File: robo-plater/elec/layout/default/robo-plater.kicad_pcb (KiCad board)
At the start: 2 copper layers, 170 parts, among them J1 ?, U1 ?, U10 ?, U11 ?, U12 ?, U13 ?, U14 ?, U15 ?, U16 ?, U17 ?, U18 ?, U19 ?, U2 ?, U20 ?, U21 ?, U22 ?, U23 ?, U24 ?, U25 ?, U26 ?, U27 ?, U28 ?, U29 ?, U3 ?, U30 ?, U31 ?, U32 ?, U33 ?, U34 ?, U35 ?, U36 ?, U37 0.6A, 42V, 1.1MHz Buck Regula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, U4 ?, U5 ?, U6 ?, U7 ?, U8 ?, U9 ?

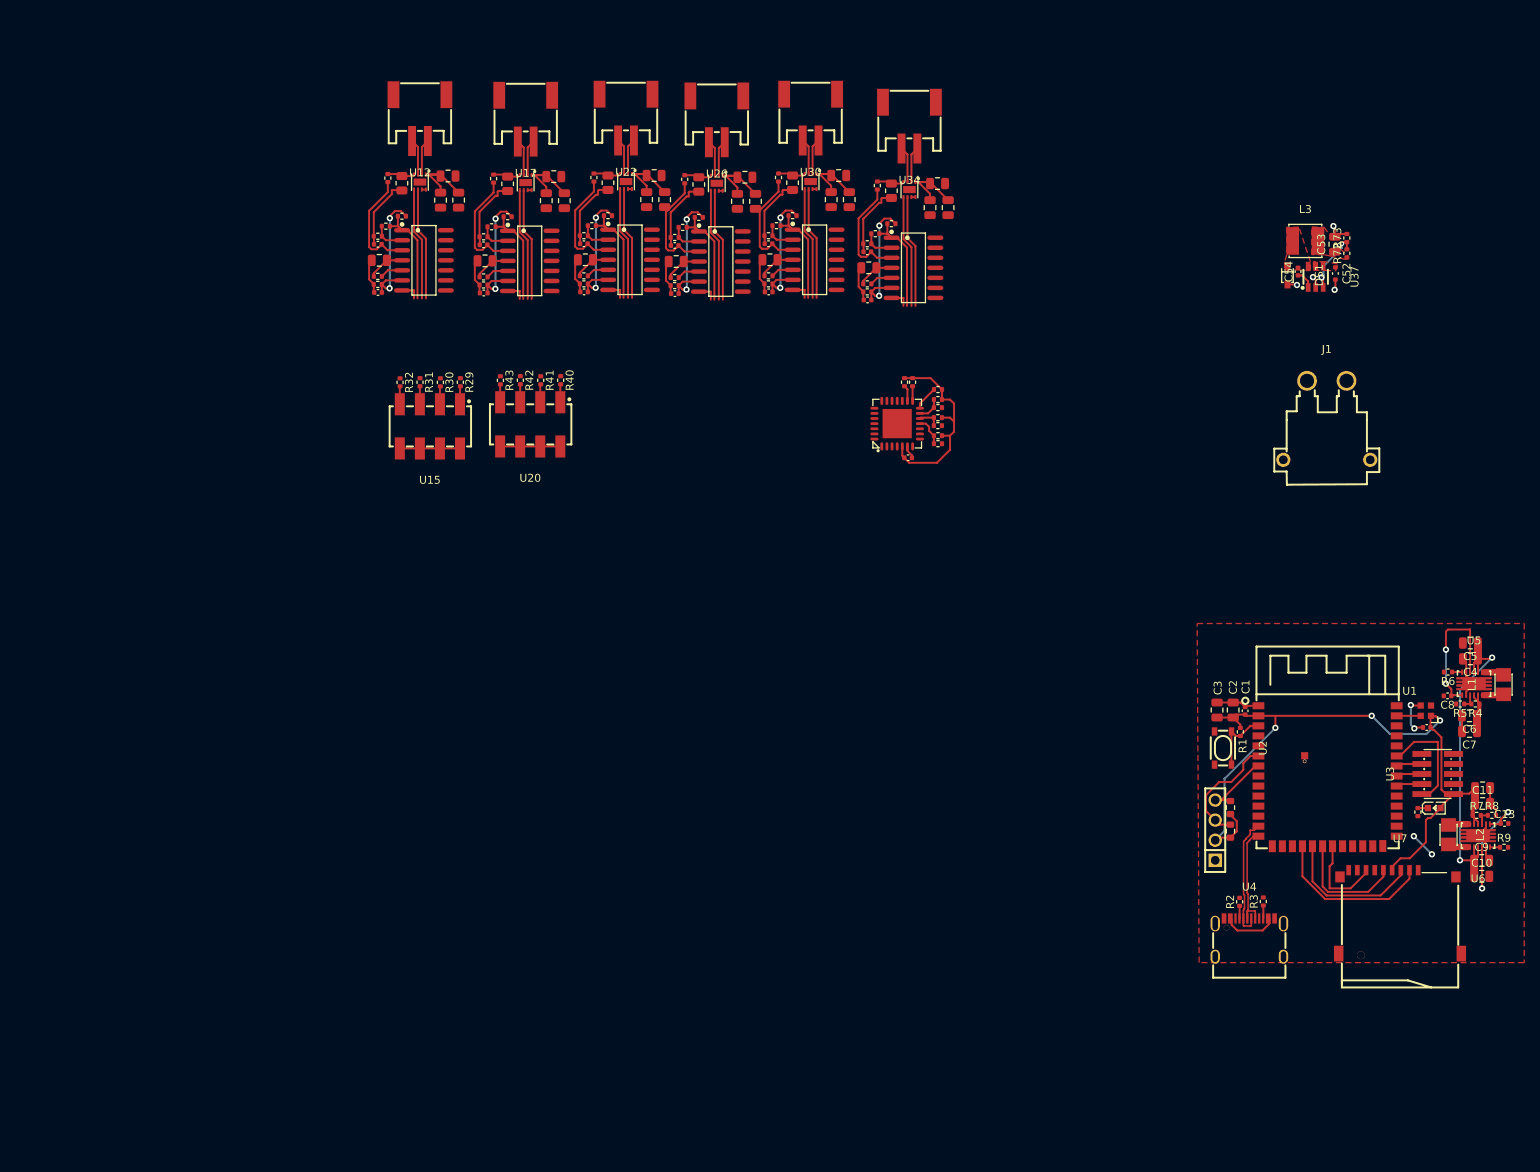
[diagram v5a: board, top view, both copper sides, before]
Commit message: Reorganise into channels
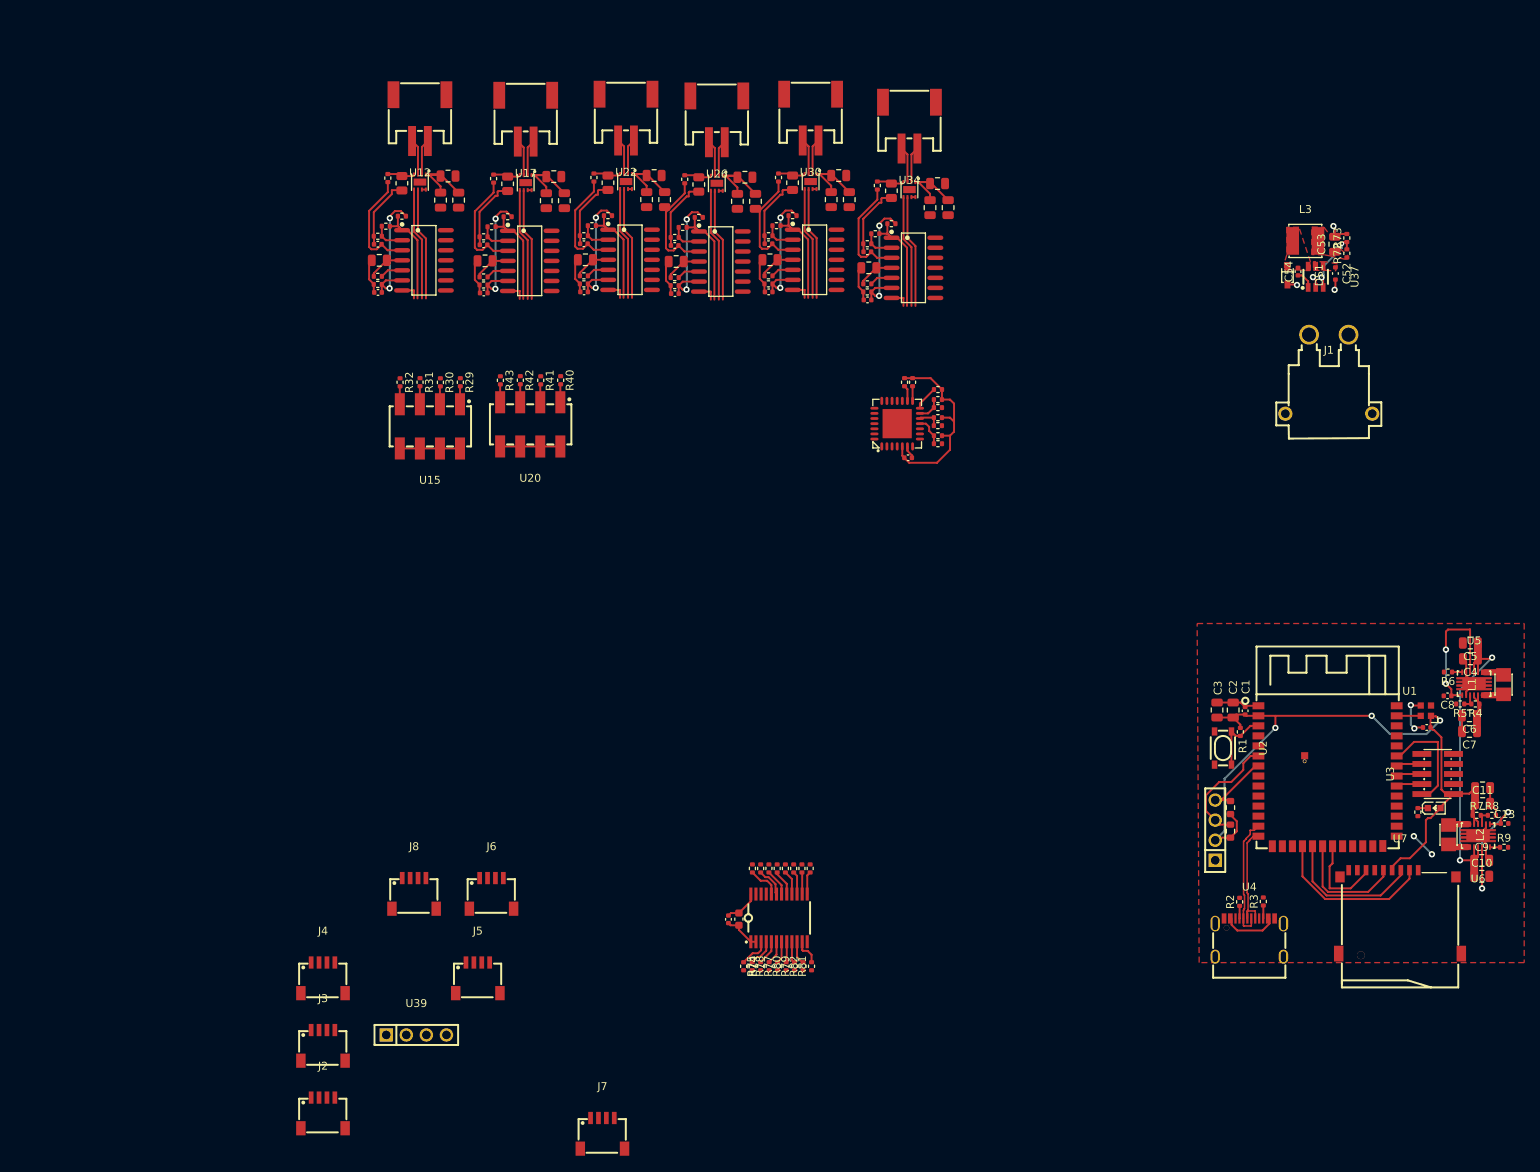
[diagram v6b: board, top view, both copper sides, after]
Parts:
- added C55: 16V 100nF X7R ±10% 0402 Multilayer Ceramic Capacitors MLCC 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, lib:C0402, F.Cu at (119.6, 149.3)
- added C56: 16V 2.2uF X5R ±10% 0603 Multilayer Ceramic Capacitors MLCC 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, lib:C0603, F.Cu at (120.9, 149.3)
- added J2: ?, lib:CONN-SMD_4P-P1.00_SM04B-SRSS-TB-LF-SN, F.Cu at (68.3, 173.8)
- added J3: ?, lib:CONN-SMD_4P-P1.00_SM04B-SRSS-TB-LF-SN, F.Cu at (68.3, 165.2)
- added J4: ?, lib:CONN-SMD_4P-P1.00_SM04B-SRSS-TB-LF-SN, F.Cu at (68.3, 156.7)
- added J5: ?, lib:CONN-SMD_4P-P1.00_SM04B-SRSS-TB-LF-SN, F.Cu at (87.9, 156.7)
- added J6: ?, lib:CONN-SMD_4P-P1.00_SM04B-SRSS-TB-LF-SN, F.Cu at (89.6, 146.0)
- added J7: ?, lib:CONN-SMD_4P-P1.00_SM04B-SRSS-TB-LF-SN, F.Cu at (103.6, 176.4)
- added J8: ?, lib:CONN-SMD_4P-P1.00_SM04B-SRSS-TB-LF-SN, F.Cu at (79.8, 146.0)
- added R74: 62.5mW Thick Film Resistors 50V ±100ppm/℃ ±1% 10kΩ 0402 Chi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, lib:R0402, F.Cu at (121.5, 155.2)
- added R75: 62.5mW Thick Film Resistors 50V ±100ppm/℃ ±1% 10kΩ 0402 Chi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, lib:R0402, F.Cu at (123.7, 155.2)
- added R76: 62.5mW Thick Film Resistors 50V ±100ppm/℃ ±1% 10kΩ 0402 Chi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, lib:R0402, F.Cu at (122.6, 155.2)
- added R77: 62.5mW Thick Film Resistors 50V ±100ppm/℃ ±1% 10kΩ 0402 Chi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, lib:R0402, F.Cu at (125.8, 155.2)
- added R78: 62.5mW Thick Film Resistors 50V ±100ppm/℃ ±1% 10kΩ 0402 Chi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, lib:R0402, F.Cu at (124.7, 155.2)
- added R79: 62.5mW Thick Film Resistors 50V ±100ppm/℃ ±1% 10kΩ 0402 Chi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, lib:R0402, F.Cu at (128.0, 155.2)
- added R80: 62.5mW Thick Film Resistors 50V ±100ppm/℃ ±1% 10kΩ 0402 Chi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, lib:R0402, F.Cu at (126.9, 155.2)
- added R81: 62.5mW Thick Film Resistors 50V ±100ppm/℃ ±1% 10kΩ 0402 Chi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, lib:R0402, F.Cu at (130.1, 155.2)
- added R82: 62.5mW Thick Film Resistors 50V ±100ppm/℃ ±1% 10kΩ 0402 Chi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, lib:R0402, F.Cu at (129.0, 155.2)
- added R83: 62.5mW Thick Film Resistors 50V ±100ppm/℃ ±1% 10kΩ 0402 Chi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, lib:R0402, F.Cu at (128.9, 142.8)
- added R84: 62.5mW Thick Film Resistors 50V ±100ppm/℃ ±1% 10kΩ 0402 Chi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, lib:R0402, F.Cu at (129.9, 142.8)
- added R85: 62.5mW Thick Film Resistors 50V ±100ppm/℃ ±1% 10kΩ 0402 Chi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, lib:R0402, F.Cu at (126.8, 142.8)
- added R86: 62.5mW Thick Film Resistors 50V ±100ppm/℃ ±1% 10kΩ 0402 Chi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, lib:R0402, F.Cu at (127.8, 142.8)
- added R87: 62.5mW Thick Film Resistors 50V ±100ppm/℃ ±1% 10kΩ 0402 Chi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, lib:R0402, F.Cu at (124.7, 142.8)
- added R88: 62.5mW Thick Film Resistors 50V ±100ppm/℃ ±1% 10kΩ 0402 Chi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, lib:R0402, F.Cu at (125.7, 142.8)
- added R89: 62.5mW Thick Film Resistors 50V ±100ppm/℃ ±1% 10kΩ 0402 Chi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, lib:R0402, F.Cu at (122.6, 142.8)
- added R90: 62.5mW Thick Film Resistors 50V ±100ppm/℃ ±1% 10kΩ 0402 Chi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, lib:R0402, F.Cu at (123.7, 142.8)
- added U38: ?, lib:TSSOP-24_L7.8-W4.4-P0.65-LS6.4-BL, F.Cu at (126.0, 149.1)
- added U39: ?, lib:HDR-TH_4P-P2.54-V-F, F.Cu at (80.1, 163.9)
- moved J1 5.84 mm to (195.6, 80.3)
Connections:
- net scl renamed uc.uc.ic-scl
- net sda renamed uc.uc.ic-sda
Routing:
- net gnd: track 87.1 -> 91.9 mm
- net vcc-1: track 149.1 -> 153.6 mm
- net i2c_mux.ic-scl-7: track 0.00 -> 4.21 mm
- net reset_: track 0.00 -> 3.91 mm
- net i2c_mux.ic-sda-7: track 0.00 -> 3.89 mm
- net i2c_mux.ic-sda: track 0.00 -> 3.51 mm
- net i2c_mux.ic-scl-3: track 0.00 -> 3.42 mm
- net i2c_mux.ic-scl-6: track 0.00 -> 3.40 mm
- net i2c_mux.ic-sda-6: track 0.00 -> 3.24 mm
- net i2c_mux.ic-scl: track 0.00 -> 3.13 mm
- net i2c_mux.ic-scl-5: track 0.00 -> 3.07 mm
- net i2c_mux.ic-sda-1: track 0.00 -> 2.99 mm
- net i2c_mux.ic-sda-3: track 0.00 -> 2.94 mm
- net i2c_mux.ic-sda-5: track 0.00 -> 2.91 mm
- net i2c_mux.ic-sda-4: track 0.00 -> 2.89 mm
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
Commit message: Add stemma/quuic connectors and load cell amps
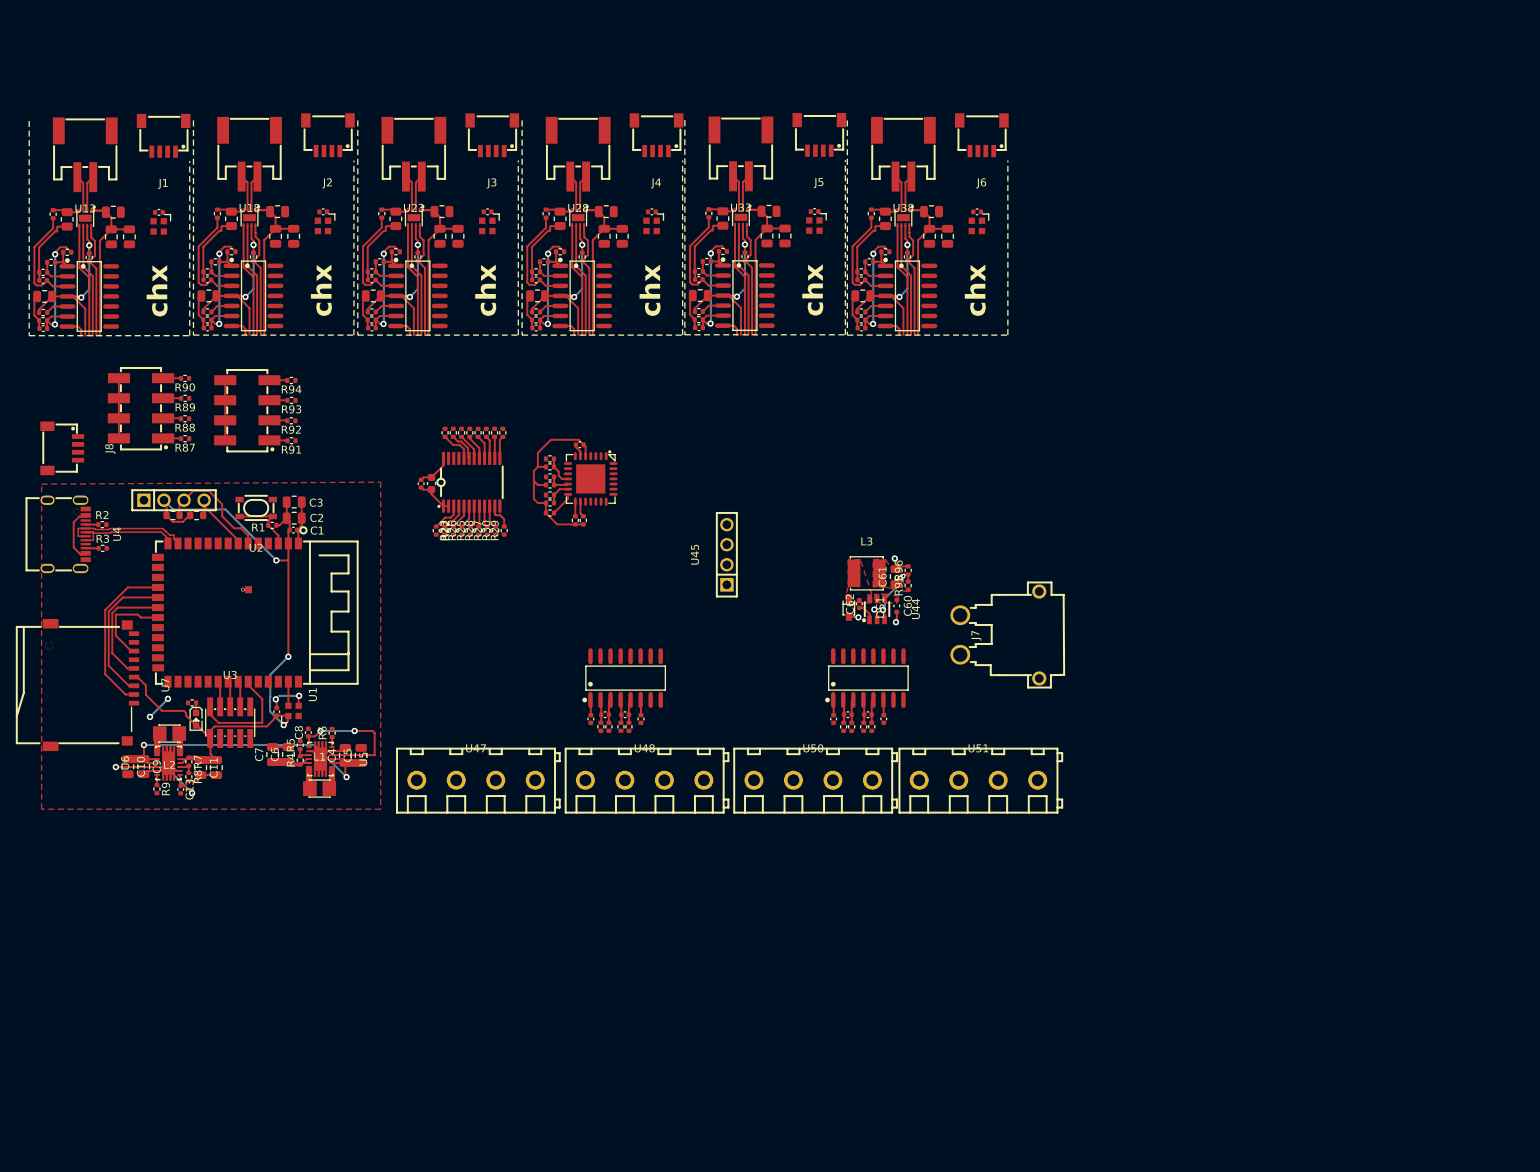
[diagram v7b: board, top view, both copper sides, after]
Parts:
- removed the J7 at (103.6, 176.4)
- removed the R87 at (124.7, 142.8)
- removed the R88 at (125.7, 142.8)
- removed the R89 at (122.6, 142.8)
- removed the R90 at (123.7, 142.8)
- added C52: 16V 100nF X7R ±10% 0402 Multilayer Ceramic Capacitors MLCC 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, lib:C0402, F.Cu at (130.5, 59.7)
- added C53: 25V 10uF X5R ±10% 0805 Multilayer Ceramic Capacitors MLCC -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, lib:C0805, F.Cu at (147.3, 62.8)
- added C54: 25V 10uF X5R ±10% 0805 Multilayer Ceramic Capacitors MLCC -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, lib:C0805, F.Cu at (145.0, 62.8)
- added C57: 16V 100nF X7R ±10% 0402 Multilayer Ceramic Capacitors MLCC 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, lib:C0402, F.Cu at (136.4, 68.3)
- added C58: 25V 1uF X5R ±10% 0402 Multilayer Ceramic Capacitors MLCC - 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, lib:C0402, F.Cu at (136.4, 74.4)
- added C59: 16V 100nF X7R ±10% 0402 Multilayer Ceramic Capacitors MLCC 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, lib:C0402, F.Cu at (151.1, 59.7)
- added C63: 16V 100nF X7R ±10% 0402 Multilayer Ceramic Capacitors MLCC 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, lib:C0402, F.Cu at (108.5, 123.9)
- added C64: 16V 100nF X7R ±10% 0402 Multilayer Ceramic Capacitors MLCC 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, lib:C0402, F.Cu at (102.2, 123.9)
- added C65: 16V 100nF X7R ±10% 0402 Multilayer Ceramic Capacitors MLCC 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, lib:C0402, F.Cu at (104.0, 123.4)
- added C66: 16V 100nF X7R ±10% 0402 Multilayer Ceramic Capacitors MLCC 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, lib:C0402, F.Cu at (106.5, 123.4)
- added C67: 16V 100nF X7R ±10% 0402 Multilayer Ceramic Capacitors MLCC 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, lib:C0402, F.Cu at (139.2, 123.9)
- added C68: 16V 100nF X7R ±10% 0402 Multilayer Ceramic Capacitors MLCC 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, lib:C0402, F.Cu at (132.9, 123.9)
- added C69: 16V 100nF X7R ±10% 0402 Multilayer Ceramic Capacitors MLCC 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, lib:C0402, F.Cu at (134.7, 123.4)
- added C70: 16V 100nF X7R ±10% 0402 Multilayer Ceramic Capacitors MLCC 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, lib:C0402, F.Cu at (137.2, 123.4)
- added J1: ?, lib:CONN-SMD_4P-P1.00_SM04B-SRSS-TB-LF-SN, F.Cu at (48.1, 50.2)
- added R100: 62.5mW Thick Film Resistors 50V ±100ppm/℃ ±1% 49.9Ω 0402 Ch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, lib:R0402, F.Cu at (107.0, 124.9)
- added R101: 62.5mW Thick Film Resistors 50V ±100ppm/℃ ±1% 49.9Ω 0402 Ch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, lib:R0402, F.Cu at (134.2, 124.9)
- added R102: 62.5mW Thick Film Resistors 50V ±100ppm/℃ ±1% 49.9Ω 0402 Ch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, lib:R0402, F.Cu at (135.2, 124.9)
- added R103: 62.5mW Thick Film Resistors 50V ±100ppm/℃ ±1% 49.9Ω 0402 Ch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, lib:R0402, F.Cu at (136.7, 124.9)
- added R104: 62.5mW Thick Film Resistors 50V ±100ppm/℃ ±1% 49.9Ω 0402 Ch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, lib:R0402, F.Cu at (137.7, 124.9)
- added R29: 62.5mW Thick Film Resistors 50V ±100ppm/℃ ±1% 10kΩ 0402 Chi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, lib:R0402, F.Cu at (91.2, 100.1)
- added R30: 62.5mW Thick Film Resistors 50V ±100ppm/℃ ±1% 10kΩ 0402 Chi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, lib:R0402, F.Cu at (90.1, 100.1)
- added R31: 62.5mW Thick Film Resistors 50V ±100ppm/℃ ±1% 10kΩ 0402 Chi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, lib:R0402, F.Cu at (90.0, 87.7)
- added R32: 62.5mW Thick Film Resistors 50V ±100ppm/℃ ±1% 10kΩ 0402 Chi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, lib:R0402, F.Cu at (91.0, 87.7)
- added R40: 125mW Thick Film Resistors 150V ±1% ±400ppm/℃ 1Ω 0805 Chip 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, lib:R0805, F.Cu at (35.9, 60.7)
- added R41: 62.5mW Thick Film Resistors 50V ±100ppm/℃ ±1% 1.33kΩ 0402 C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, lib:R0402, F.Cu at (34.1, 60.0)
- added R42: 62.5mW Thick Film Resistors 50V ±100ppm/℃ ±1% 365Ω 0402 Chi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, lib:R0402, F.Cu at (33.8, 66.1)
- added R43: 62.5mW Thick Film Resistors 50V ±100ppm/℃ ±1% 36.5Ω 0402 Ch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, lib:R0402, F.Cu at (32.8, 67.4)
- added R72: 125mW Thick Film Resistors 150V ±1% ±400ppm/℃ 1Ω 0805 Chip 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, lib:R0805, F.Cu at (118.9, 60.6)
- added R73: 62.5mW Thick Film Resistors 50V ±100ppm/℃ ±1% 1.33kΩ 0402 C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, lib:R0402, F.Cu at (117.1, 59.9)
- added R97: 62.5mW Thick Film Resistors 50V ±100ppm/℃ ±1% 49.9Ω 0402 Ch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, lib:R0402, F.Cu at (103.4, 124.9)
- added R98: 62.5mW Thick Film Resistors 50V ±100ppm/℃ ±1% 49.9Ω 0402 Ch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, lib:R0402, F.Cu at (104.4, 124.9)
- added R99: 62.5mW Thick Film Resistors 50V ±100ppm/℃ ±1% 49.9Ω 0402 Ch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, lib:R0402, F.Cu at (106.0, 124.9)
- added U15: ?, lib:SOIC-14_L8.7-W3.9-P1.27-LS6.0-BL, F.Cu at (38.7, 70.4)
- added U20: ?, lib:SOIC-14_L8.7-W3.9-P1.27-LS6.0-BL, F.Cu at (59.5, 70.4)
- added U37: ?, lib:WSON-8_L2.0-W2.0-P0.50-TL-EP, F.Cu at (141.7, 60.5)
- added U39: ?, lib:NetTie-2_SMD_Pad0.25mm, F.Cu at (138.2, 62.1)
- added U40: ?, lib:SOIC-14_L8.7-W3.9-P1.27-LS6.0-BL, F.Cu at (142.2, 70.4)
- added U41: ?, lib:LED-SMD_4P-L2.0-W2.0-BR, F.Cu at (151.0, 61.5)
- added U46: ?, lib:SOP-16_L9.9-W3.9-P1.27-LS6.0-BL, F.Cu at (106.6, 118.7)
- added U47: ?, lib:CONN-TH_4P-P5.00_DB127V-5.0-4P-GN-S, F.Cu at (87.6, 131.7)
- added U48: ?, lib:CONN-TH_4P-P5.00_DB127V-5.0-4P-GN-S, F.Cu at (109.0, 131.7)
- added U49: ?, lib:SOP-16_L9.9-W3.9-P1.27-LS6.0-BL, F.Cu at (137.3, 118.7)
- added U50: ?, lib:CONN-TH_4P-P5.00_DB127V-5.0-4P-GN-S, F.Cu at (130.3, 131.7)
- added U51: ?, lib:CONN-TH_4P-P5.00_DB127V-5.0-4P-GN-S, F.Cu at (151.2, 131.7)
- C16, C22, C24, C29, C31, C36, C43: value 25V 10uF X5R ±10% 0805 Multilayer Ceramic Capacitors MLCC - SMD/SMT ROHS -> 16V 100nF X7R ±10% 0402 Multilayer Ceramic Capacitors MLCC - SMD/SMT ROHS; footprint lib:C0805 -> lib:C0402
- C17: value 25V 10uF X5R ±10% 0805 Multilayer Ceramic Capacitors MLCC - SMD/SMT ROHS -> 16V 2.2uF X5R ±10% 0603 Multilayer Ceramic Capacitors MLCC - SMD/SMT ROHS; footprint lib:C0805 -> lib:C0603
- C20, C26, C32, C55: value 16V 100nF X7R ±10% 0402 Multilayer Ceramic Capacitors MLCC - SMD/SMT ROHS -> 25V 10uF X5R ±10% 0805 Multilayer Ceramic Capacitors MLCC - SMD/SMT ROHS; footprint lib:C0402 -> lib:C0805
- C21, C27, C33, C39: value 25V 1uF X5R ±10% 0402 Multilayer Ceramic Capacitors MLCC - SMD/SMT ROHS -> 25V 10uF X5R ±10% 0805 Multilayer Ceramic Capacitors MLCC - SMD/SMT ROHS; footprint lib:C0402 -> lib:C0805
- C23, C30, C37: value 25V 10uF X5R ±10% 0805 Multilayer Ceramic Capacitors MLCC - SMD/SMT ROHS -> 25V 1uF X5R ±10% 0402 Multilayer Ceramic Capacitors MLCC - SMD/SMT ROHS; footprint lib:C0805 -> lib:C0402
- C44: value 16V 100nF X7R ±10% 0402 Multilayer Ceramic Capacitors MLCC - SMD/SMT ROHS -> 25V 1uF X5R ±10% 0402 Multilayer Ceramic Capacitors MLCC - SMD/SMT ROHS
- C45: value 25V 1uF X5R ±10% 0402 Multilayer Ceramic Capacitors MLCC - SMD/SMT ROHS -> 16V 100nF X7R ±10% 0402 Multilayer Ceramic Capacitors MLCC - SMD/SMT ROHS
- C56: value 16V 2.2uF X5R ±10% 0603 Multilayer Ceramic Capacitors MLCC - SMD/SMT ROHS -> 25V 10uF X5R ±10% 0805 Multilayer Ceramic Capacitors MLCC - SMD/SMT ROHS; footprint lib:C0603 -> lib:C0805
- R22, R33: value 125mW Thick Film Resistors 150V ±1% ±400ppm/℃ 1Ω 0805 Chip Resistor - Surface Mount ROHS -> 62.5mW Thick Film Resistors 50V ±100ppm/℃ ±1% 10kΩ 0402 Chip Resistor - Surface Mount ROHS; footprint lib:R0805 -> lib:R0402
- R23, R34: value 62.5mW Thick Film Resistors 50V ±100ppm/℃ ±1% 1.33kΩ 0402 Chip Resistor - Surface Mount ROHS -> 62.5mW Thick Film Resistors 50V ±100ppm/℃ ±1% 10kΩ 0402 Chip Resistor - Surface Mount ROHS
- R24, R35: value 62.5mW Thick Film Resistors 50V ±100ppm/℃ ±1% 365Ω 0402 Chip Resistor - Surface Mount ROHS -> 62.5mW Thick Film Resistors 50V ±100ppm/℃ ±1% 10kΩ 0402 Chip Resistor - Surface Mount ROHS
- R25, R36, R47: value 62.5mW Thick Film Resistors 50V ±100ppm/℃ ±1% 36.5Ω 0402 Chip Resistor - Surface Mount ROHS -> 62.5mW Thick Film Resistors 50V ±100ppm/℃ ±1% 10kΩ 0402 Chip Resistor - Surface Mount ROHS
- R26, R37, R55: value 62.5mW Thick Film Resistors 50V ±100ppm/℃ ±1% 1.05kΩ 0402 Chip Resistor - Surface Mount ROHS -> 62.5mW Thick Film Resistors 50V ±100ppm/℃ ±1% 10kΩ 0402 Chip Resistor - Surface Mount ROHS
- R27, R28, R38, R39, R63, R71: value 62.5mW Thick Film Resistors 50V ±100ppm/℃ ±1% 1MΩ 0402 Chip Resistor - Surface Mount ROHS -> 62.5mW Thick Film Resistors 50V ±100ppm/℃ ±1% 10kΩ 0402 Chip Resistor - Surface Mount ROHS
- R44: value 125mW Thick Film Resistors 150V ±1% ±400ppm/℃ 1Ω 0805 Chip Resistor - Surface Mount ROHS -> 62.5mW Thick Film Resistors 50V ±100ppm/℃ ±1% 1.05kΩ 0402 Chip Resistor - Surface Mount ROHS; footprint lib:R0805 -> lib:R0402
- R45: value 62.5mW Thick Film Resistors 50V ±100ppm/℃ ±1% 1.33kΩ 0402 Chip Resistor - Surface Mount ROHS -> 62.5mW Thick Film Resistors 50V ±100ppm/℃ ±1% 1MΩ 0402 Chip Resistor - Surface Mount ROHS
- R46, R53: value 62.5mW Thick Film Resistors 50V ±100ppm/℃ ±1% 365Ω 0402 Chip Resistor - Surface Mount ROHS -> 62.5mW Thick Film Resistors 50V ±100ppm/℃ ±1% 1MΩ 0402 Chip Resistor - Surface Mount ROHS
- R48: value 62.5mW Thick Film Resistors 50V ±100ppm/℃ ±1% 1.05kΩ 0402 Chip Resistor - Surface Mount ROHS -> 125mW Thick Film Resistors 150V ±1% ±400ppm/℃ 1Ω 0805 Chip Resistor - Surface Mount ROHS; footprint lib:R0402 -> lib:R0805
- R49, R57: value 62.5mW Thick Film Resistors 50V ±100ppm/℃ ±1% 1MΩ 0402 Chip Resistor - Surface Mount ROHS -> 62.5mW Thick Film Resistors 50V ±100ppm/℃ ±1% 1.33kΩ 0402 Chip Resistor - Surface Mount ROHS
- R50: value 62.5mW Thick Film Resistors 50V ±100ppm/℃ ±1% 1MΩ 0402 Chip Resistor - Surface Mount ROHS -> 62.5mW Thick Film Resistors 50V ±100ppm/℃ ±1% 365Ω 0402 Chip Resistor - Surface Mount ROHS
- R51: value 125mW Thick Film Resistors 150V ±1% ±400ppm/℃ 1Ω 0805 Chip Resistor - Surface Mount ROHS -> 62.5mW Thick Film Resistors 50V ±100ppm/℃ ±1% 36.5Ω 0402 Chip Resistor - Surface Mount ROHS; footprint lib:R0805 -> lib:R0402
- R52: value 62.5mW Thick Film Resistors 50V ±100ppm/℃ ±1% 1.33kΩ 0402 Chip Resistor - Surface Mount ROHS -> 62.5mW Thick Film Resistors 50V ±100ppm/℃ ±1% 1.05kΩ 0402 Chip Resistor - Surface Mount ROHS
- R54, R61: value 62.5mW Thick Film Resistors 50V ±100ppm/℃ ±1% 36.5Ω 0402 Chip Resistor - Surface Mount ROHS -> 62.5mW Thick Film Resistors 50V ±100ppm/℃ ±1% 1MΩ 0402 Chip Resistor - Surface Mount ROHS
- R56, R64: value 62.5mW Thick Film Resistors 50V ±100ppm/℃ ±1% 1MΩ 0402 Chip Resistor - Surface Mount ROHS -> 125mW Thick Film Resistors 150V ±1% ±400ppm/℃ 1Ω 0805 Chip Resistor - Surface Mount ROHS; footprint lib:R0402 -> lib:R0805
- R58: value 125mW Thick Film Resistors 150V ±1% ±400ppm/℃ 1Ω 0805 Chip Resistor - Surface Mount ROHS -> 62.5mW Thick Film Resistors 50V ±100ppm/℃ ±1% 365Ω 0402 Chip Resistor - Surface Mount ROHS; footprint lib:R0805 -> lib:R0402
- R59: value 62.5mW Thick Film Resistors 50V ±100ppm/℃ ±1% 1.33kΩ 0402 Chip Resistor - Surface Mount ROHS -> 62.5mW Thick Film Resistors 50V ±100ppm/℃ ±1% 36.5Ω 0402 Chip Resistor - Surface Mount ROHS
- R60: value 62.5mW Thick Film Resistors 50V ±100ppm/℃ ±1% 365Ω 0402 Chip Resistor - Surface Mount ROHS -> 62.5mW Thick Film Resistors 50V ±100ppm/℃ ±1% 1.05kΩ 0402 Chip Resistor - Surface Mount ROHS
- R62, R69: value 62.5mW Thick Film Resistors 50V ±100ppm/℃ ±1% 1.05kΩ 0402 Chip Resistor - Surface Mount ROHS -> 62.5mW Thick Film Resistors 50V ±100ppm/℃ ±1% 1MΩ 0402 Chip Resistor - Surface Mount ROHS
- R65: value 125mW Thick Film Resistors 150V ±1% ±400ppm/℃ 1Ω 0805 Chip Resistor - Surface Mount ROHS -> 62.5mW Thick Film Resistors 50V ±100ppm/℃ ±1% 1.33kΩ 0402 Chip Resistor - Surface Mount ROHS; footprint lib:R0805 -> lib:R0402
- R66: value 62.5mW Thick Film Resistors 50V ±100ppm/℃ ±1% 1.33kΩ 0402 Chip Resistor - Surface Mount ROHS -> 62.5mW Thick Film Resistors 50V ±100ppm/℃ ±1% 365Ω 0402 Chip Resistor - Surface Mount ROHS
- R67: value 62.5mW Thick Film Resistors 50V ±100ppm/℃ ±1% 365Ω 0402 Chip Resistor - Surface Mount ROHS -> 62.5mW Thick Film Resistors 50V ±100ppm/℃ ±1% 36.5Ω 0402 Chip Resistor - Surface Mount ROHS
- R68: value 62.5mW Thick Film Resistors 50V ±100ppm/℃ ±1% 36.5Ω 0402 Chip Resistor - Surface Mount ROHS -> 62.5mW Thick Film Resistors 50V ±100ppm/℃ ±1% 1.05kΩ 0402 Chip Resistor - Surface Mount ROHS
- R74, R82: value 62.5mW Thick Film Resistors 50V ±100ppm/℃ ±1% 10kΩ 0402 Chip Resistor - Surface Mount ROHS -> 62.5mW Thick Film Resistors 50V ±100ppm/℃ ±1% 365Ω 0402 Chip Resistor - Surface Mount ROHS
- R75, R83: value 62.5mW Thick Film Resistors 50V ±100ppm/℃ ±1% 10kΩ 0402 Chip Resistor - Surface Mount ROHS -> 62.5mW Thick Film Resistors 50V ±100ppm/℃ ±1% 36.5Ω 0402 Chip Resistor - Surface Mount ROHS
- R76, R84: value 62.5mW Thick Film Resistors 50V ±100ppm/℃ ±1% 10kΩ 0402 Chip Resistor - Surface Mount ROHS -> 62.5mW Thick Film Resistors 50V ±100ppm/℃ ±1% 1.05kΩ 0402 Chip Resistor - Surface Mount ROHS
- R77, R78, R85, R86: value 62.5mW Thick Film Resistors 50V ±100ppm/℃ ±1% 10kΩ 0402 Chip Resistor - Surface Mount ROHS -> 62.5mW Thick Film Resistors 50V ±100ppm/℃ ±1% 1MΩ 0402 Chip Resistor - Surface Mount ROHS
- R80: value 62.5mW Thick Film Resistors 50V ±100ppm/℃ ±1% 10kΩ 0402 Chip Resistor - Surface Mount ROHS -> 125mW Thick Film Resistors 150V ±1% ±400ppm/℃ 1Ω 0805 Chip Resistor - Surface Mount ROHS; footprint lib:R0402 -> lib:R0805
- R81: value 62.5mW Thick Film Resistors 50V ±100ppm/℃ ±1% 10kΩ 0402 Chip Resistor - Surface Mount ROHS -> 62.5mW Thick Film Resistors 50V ±100ppm/℃ ±1% 1.33kΩ 0402 Chip Resistor - Surface Mount ROHS
- U11: footprint lib:WSON-8_L2.0-W2.0-P0.50-TL-EP -> lib:TSSOP-24_L7.8-W4.4-P0.65-LS6.4-BL
- U12, U17, U22: footprint lib:CONN-SMD_P2.00_S2B-PH-SM4-TB-LF-SN -> lib:WSON-8_L2.0-W2.0-P0.50-TL-EP
- U13, U18, U23: footprint lib:NetTie-2_SMD_Pad0.25mm -> lib:CONN-SMD_P2.00_S2B-PH-SM4-TB-LF-SN
- U14, U19, U24: footprint lib:SOIC-14_L8.7-W3.9-P1.27-LS6.0-BL -> lib:NetTie-2_SMD_Pad0.25mm
- U16, U21: footprint lib:WSON-8_L2.0-W2.0-P0.50-TL-EP -> lib:LED-SMD_4P-L2.0-W2.0-BR
- U25: footprint lib:WSON-8_L2.0-W2.0-P0.50-TL-EP -> lib:SOIC-14_L8.7-W3.9-P1.27-LS6.0-BL
- U26: footprint lib:CONN-SMD_P2.00_S2B-PH-SM4-TB-LF-SN -> lib:LED-SMD_4P-L2.0-W2.0-BR
- U27: footprint lib:NetTie-2_SMD_Pad0.25mm -> lib:WSON-8_L2.0-W2.0-P0.50-TL-EP
- U28: footprint lib:SOIC-14_L8.7-W3.9-P1.27-LS6.0-BL -> lib:CONN-SMD_P2.00_S2B-PH-SM4-TB-LF-SN
- U29: footprint lib:WSON-8_L2.0-W2.0-P0.50-TL-EP -> lib:NetTie-2_SMD_Pad0.25mm
- U30: footprint lib:CONN-SMD_P2.00_S2B-PH-SM4-TB-LF-SN -> lib:SOIC-14_L8.7-W3.9-P1.27-LS6.0-BL
- U31: footprint lib:NetTie-2_SMD_Pad0.25mm -> lib:LED-SMD_4P-L2.0-W2.0-BR
- U32: footprint lib:SOIC-14_L8.7-W3.9-P1.27-LS6.0-BL -> lib:WSON-8_L2.0-W2.0-P0.50-TL-EP
- U33: footprint lib:WSON-8_L2.0-W2.0-P0.50-TL-EP -> lib:CONN-SMD_P2.00_S2B-PH-SM4-TB-LF-SN
- U34: footprint lib:CONN-SMD_P2.00_S2B-PH-SM4-TB-LF-SN -> lib:NetTie-2_SMD_Pad0.25mm
- U35: footprint lib:NetTie-2_SMD_Pad0.25mm -> lib:SOIC-14_L8.7-W3.9-P1.27-LS6.0-BL
- U36: footprint lib:SOIC-14_L8.7-W3.9-P1.27-LS6.0-BL -> lib:LED-SMD_4P-L2.0-W2.0-BR
- U38: footprint lib:TSSOP-24_L7.8-W4.4-P0.65-LS6.4-BL -> lib:CONN-SMD_P2.00_S2B-PH-SM4-TB-LF-SN
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- renumbered C52 to C60, C53 to C61, C54 to C62, J1 to J7, R29 to R87, R30 to R88, R31 to R89, R32 to R90, R40 to R91, R41 to R92, R42 to R93, R43 to R94, R72 to R95, R73 to R96, U15 to U42, U20 to U43, U37 to U44, U39 to U45
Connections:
- net ch4.driver-ep renamed ch3.motor_driver.op_amp-in3_minus
- net ch5.op_amp-in3_minus renamed ch5.motor_driver.driver-ep
- C1 pad 1: vcc-1 -> vcc-2
- C11 pad 1: vcc-1 -> vcc-2
- C12 pad 1: vcc-1 -> vcc-2
- C14 pad 1: vcc-1 -> vcc-2
- C15 pad 1: vcc-1 -> vcc-2
- C16 pad 1: vcc -> vcc-2
- C17 pad 1: vcc -> vcc-2
- C19 pad 1: vcc-1 -> vcc
- C2 pad 1: vcc-1 -> vcc-2
- C20 pad 1: ch1.op_amp-in1_plus -> vcc
- C20 pad 2: ch1._shunt_nettie-_shunt_gnd -> gnd
- C21 pad 1: ch1.op_amp-in2_minus -> vcc-2
- C22 pad 1: vcc -> ch1.motor_driver.op_amp-in1_plus
- C22 pad 2: gnd -> ch1.motor_driver._shunt_nettie-_shunt_gnd
- C23 pad 1: vcc -> ch1.motor_driver.op_amp-in2_minus
- C24 pad 1: vcc -> vcc-1
- C25 pad 1: vcc-1 -> vcc
- C26 pad 1: ch2.op_amp-in1_plus -> vcc
- C26 pad 2: ch2._shunt_nettie-_shunt_gnd -> gnd
- C27 pad 1: ch2.op_amp-in2_minus -> vcc
- C28 pad 1: vcc -> vcc-2
- C29 pad 1: vcc -> ch2.motor_driver.op_amp-in1_plus
- C29 pad 2: gnd -> ch2.motor_driver._shunt_nettie-_shunt_gnd
- C3 pad 1: vcc-1 -> vcc-2
- C30 pad 1: vcc -> ch2.motor_driver.op_amp-in2_minus
- C32 pad 1: ch3.op_amp-in1_plus -> vcc
- C32 pad 2: ch3._shunt_nettie-_shunt_gnd -> gnd
- C33 pad 1: ch3.op_amp-in2_minus -> vcc
- C35 pad 1: vcc -> vcc-2
- C36 pad 1: vcc -> ch3.motor_driver.op_amp-in1_plus
- C36 pad 2: gnd -> ch3.motor_driver._shunt_nettie-_shunt_gnd
- C37 pad 1: vcc-1 -> ch3.motor_driver.op_amp-in2_minus
- C38 pad 1: ch4.op_amp-in1_plus -> vcc-1
- C38 pad 2: ch4._shunt_nettie-_shunt_gnd -> gnd
- C39 pad 1: ch4.op_amp-in2_minus -> vcc
- C42 pad 1: vcc -> vcc-2
- C43 pad 1: vcc-1 -> ch4.motor_driver.op_amp-in1_plus
- C43 pad 2: gnd -> ch4.motor_driver._shunt_nettie-_shunt_gnd
- C44 pad 1: ch5.op_amp-in1_plus -> ch4.motor_driver.op_amp-in2_minus
- C44 pad 2: ch5._shunt_nettie-_shunt_gnd -> gnd
- C45 pad 1: ch5.op_amp-in2_minus -> vcc-1
- C49 pad 1: vcc-1 -> vcc-2
- C50 pad 1: ch6.op_amp-in1_plus -> ch5.motor_driver.op_amp-in1_plus
- C50 pad 2: ch6._shunt_nettie-_shunt_gnd -> ch5.motor_driver._shunt_nettie-_shunt_gnd
- C51 pad 1: ch6.op_amp-in2_minus -> ch5.motor_driver.op_amp-in2_minus
- C55 pad 1: vcc-1 -> vcc
- C56 pad 1: vcc-1 -> vcc-2
- C6 pad 1: uc._5v_reg-vcc -> vcc-1
- C7 pad 1: uc._5v_reg-vcc -> vcc-1
- J2 pad 2: vcc-1 -> vcc-2
- J2 pad 3: i2c_mux.ic-sda -> i2c_mux.ic-sda-1
- J2 pad 4: i2c_mux.ic-scl -> i2c_mux.ic-scl-1
- J3 pad 2: vcc-1 -> vcc-2
- J3 pad 3: i2c_mux.ic-sda-1 -> i2c_mux.ic-sda-2
- J3 pad 4: i2c_mux.ic-scl-1 -> i2c_mux.ic-scl-2
- J4 pad 2: vcc-1 -> vcc-2
- J4 pad 3: i2c_mux.ic-sda-2 -> i2c_mux.ic-sda-3
- J4 pad 4: i2c_mux.ic-scl-2 -> i2c_mux.ic-scl-3
- J5 pad 2: vcc-1 -> vcc-2
- J5 pad 3: i2c_mux.ic-sda-3 -> i2c_mux.ic-sda-4
- J5 pad 4: i2c_mux.ic-scl-3 -> i2c_mux.ic-scl-4
- J6 pad 2: vcc-1 -> vcc-2
- J6 pad 3: i2c_mux.ic-sda-4 -> i2c_mux.ic-sda-5
- J6 pad 4: i2c_mux.ic-scl-4 -> i2c_mux.ic-scl-5
- J8 pad 2: vcc-1 -> vcc-2
- LED1 pad 2: vcc-1 -> vcc-2
- R1 pad 1: vcc-1 -> vcc-2
- R11 pad 2: vcc-1 -> vcc-2
- R12 pad 2: vcc-1 -> vcc-2
- R13 pad 1: vcc-1 -> vcc-2
- R15 pad 1: vcc-1 -> vcc-2
- R17 pad 1: vcc-1 -> vcc-2
- R19 pad 1: vcc-1 -> vcc-2
- R20 pad 1: vcc-1 -> vcc-2
- R21 pad 1: vcc-1 -> vcc-2
- R22 pad 1: ch1.driver-_shunt_high -> reset_
- R22 pad 2: gnd -> vcc-2
- R23 pad 1: ch1.driver-_shunt_high -> vcc-2
- R23 pad 2: ch1.op_amp-in1_plus -> i2c_mux.ic-scl
- R24 pad 1: ch1.current -> vcc-2
- R24 pad 2: ch1.op_amp-in1_minus -> i2c_mux.ic-sda
- R25 pad 1: ch1.op_amp-in1_minus -> vcc-2
- R25 pad 2: ch1._shunt_nettie-_shunt_gnd -> i2c_mux.ic-scl-1
- R26 pad 1: ch1.current -> vcc-2
- R26 pad 2: ch1.op_amp-in2_minus -> i2c_mux.ic-sda-1
- R27 pad 1: ch1.op_amp-in2_plus -> vcc-2
- R27 pad 2: vcc-1 -> i2c_mux.ic-scl-2
- R28 pad 1: ch1.op_amp-in2_minus -> vcc-2
- R28 pad 2: gnd -> i2c_mux.ic-sda-2
- R33 pad 1: ch2.driver-_shunt_high -> vcc-2
- R33 pad 2: gnd -> i2c_mux.ic-scl-5
- R34 pad 1: ch2.driver-_shunt_high -> vcc-2
- R34 pad 2: ch2.op_amp-in1_plus -> i2c_mux.ic-sda-5
- R35 pad 1: ch2.current -> vcc-2
- R35 pad 2: ch2.op_amp-in1_minus -> i2c_mux.ic-scl-6
- R36 pad 1: ch2.op_amp-in1_minus -> vcc-2
- R36 pad 2: ch2._shunt_nettie-_shunt_gnd -> i2c_mux.ic-sda-6
- R37 pad 1: ch2.current -> vcc-2
- R37 pad 2: ch2.op_amp-in2_minus -> i2c_mux.ic-scl-7
- R38 pad 1: ch2.op_amp-in2_plus -> vcc-2
- R38 pad 2: vcc-1 -> i2c_mux.ic-sda-7
- R39 pad 1: ch2.op_amp-in2_minus -> ch1.motor_driver-enable
- R39 pad 2: gnd -> vcc-2
- R4 pad 1: uc._5v_reg-vcc -> vcc-1
- R44 pad 1: ch3.driver-_shunt_high -> ch1.current
- R44 pad 2: gnd -> ch1.motor_driver.op_amp-in2_minus
- R45 pad 1: ch3.driver-_shunt_high -> ch1.motor_driver.op_amp-in2_plus
- R45 pad 2: ch3.op_amp-in1_plus -> vcc-2
- R46 pad 1: ch3-current -> ch1.motor_driver.op_amp-in2_minus
- R46 pad 2: ch3.op_amp-in1_minus -> gnd
- R47 pad 1: ch3.op_amp-in1_minus -> ch2.motor_driver-enable
- R47 pad 2: ch3._shunt_nettie-_shunt_gnd -> vcc-2
- R48 pad 1: ch3-current -> ch2.motor_driver.driver-_shunt_high
- R48 pad 2: ch3.op_amp-in2_minus -> gnd
- R49 pad 1: ch3.op_amp-in2_plus -> ch2.motor_driver.driver-_shunt_high
- R49 pad 2: vcc-1 -> ch2.motor_driver.op_amp-in1_plus
- R50 pad 1: ch3.op_amp-in2_minus -> ch2.current
- R50 pad 2: gnd -> ch2.motor_driver.op_amp-in1_minus
- R51 pad 1: ch4.driver-_shunt_high -> ch2.motor_driver.op_amp-in1_minus
- R51 pad 2: gnd -> ch2.motor_driver._shunt_nettie-_shunt_gnd
- R52 pad 1: ch4.driver-_shunt_high -> ch2.current
- R52 pad 2: ch4.op_amp-in1_plus -> ch2.motor_driver.op_amp-in2_minus
- R53 pad 1: ch4-current -> ch2.motor_driver.op_amp-in2_plus
- R53 pad 2: ch4.op_amp-in1_minus -> vcc-2
- R54 pad 1: ch4.op_amp-in1_minus -> ch2.motor_driver.op_amp-in2_minus
- R54 pad 2: ch4._shunt_nettie-_shunt_gnd -> gnd
- R55 pad 1: ch4-current -> ch3.motor_driver-enable
- R55 pad 2: ch4.op_amp-in2_minus -> vcc-2
- R56 pad 1: ch4.op_amp-in2_plus -> ch3.motor_driver.driver-_shunt_high
- R56 pad 2: vcc-1 -> gnd
- R57 pad 1: ch4.op_amp-in2_minus -> ch3.motor_driver.driver-_shunt_high
- R57 pad 2: gnd -> ch3.motor_driver.op_amp-in1_plus
- R58 pad 1: ch5.driver-_shunt_high -> ch3.motor_driver-current
- R58 pad 2: gnd -> ch3.motor_driver.op_amp-in1_minus
- R59 pad 1: ch5.driver-_shunt_high -> ch3.motor_driver.op_amp-in1_minus
- R59 pad 2: ch5.op_amp-in1_plus -> ch3.motor_driver._shunt_nettie-_shunt_gnd
- R60 pad 1: ch5-current -> ch3.motor_driver-current
- R60 pad 2: ch5.op_amp-in1_minus -> ch3.motor_driver.op_amp-in2_minus
- R61 pad 1: ch5.op_amp-in1_minus -> ch3.motor_driver.op_amp-in2_plus
- R61 pad 2: ch5._shunt_nettie-_shunt_gnd -> vcc-2
- R62 pad 1: ch5-current -> ch3.motor_driver.op_amp-in2_minus
- R62 pad 2: ch5.op_amp-in2_minus -> gnd
- R63 pad 1: ch5.op_amp-in2_plus -> ch4.motor_driver-enable
- R63 pad 2: vcc-1 -> vcc-2
- R64 pad 1: ch5.op_amp-in2_minus -> ch4.motor_driver.driver-_shunt_high
- R65 pad 1: ch6.driver-_shunt_high -> ch4.motor_driver.driver-_shunt_high
- R65 pad 2: gnd -> ch4.motor_driver.op_amp-in1_plus
- R66 pad 1: ch6.driver-_shunt_high -> ch4.motor_driver-current
- R66 pad 2: ch6.op_amp-in1_plus -> ch4.motor_driver.op_amp-in1_minus
- R67 pad 1: ch6-current -> ch4.motor_driver.op_amp-in1_minus
- R67 pad 2: ch6.op_amp-in1_minus -> ch4.motor_driver._shunt_nettie-_shunt_gnd
- R68 pad 1: ch6.op_amp-in1_minus -> ch4.motor_driver-current
- R68 pad 2: ch6._shunt_nettie-_shunt_gnd -> ch4.motor_driver.op_amp-in2_minus
- R69 pad 1: ch6-current -> ch4.motor_driver.op_amp-in2_plus
- R69 pad 2: ch6.op_amp-in2_minus -> vcc-2
- R7 pad 1: vcc-1 -> vcc-2
- R70 pad 1: ch6.op_amp-in2_plus -> ch4.motor_driver.op_amp-in2_minus
- R70 pad 2: vcc-1 -> gnd
- R71 pad 1: ch6.op_amp-in2_minus -> ch5.motor_driver-enable
- R71 pad 2: gnd -> vcc-2
- R74 pad 1: reset_ -> ch5.motor_driver-current
- R74 pad 2: vcc-1 -> ch5.motor_driver.op_amp-in1_minus
- R75 pad 1: vcc-1 -> ch5.motor_driver.op_amp-in1_minus
- R75 pad 2: i2c_mux.ic-scl -> ch5.motor_driver._shunt_nettie-_shunt_gnd
- R76 pad 1: vcc-1 -> ch5.motor_driver-current
- R76 pad 2: i2c_mux.ic-sda -> ch5.motor_driver.op_amp-in2_minus
- R77 pad 1: vcc-1 -> ch5.motor_driver.op_amp-in2_plus
- R77 pad 2: i2c_mux.ic-scl-1 -> vcc-2
- R78 pad 1: vcc-1 -> ch5.motor_driver.op_amp-in2_minus
- R78 pad 2: i2c_mux.ic-sda-1 -> gnd
- R79 pad 1: vcc-1 -> ch6.motor_driver-enable
- R79 pad 2: i2c_mux.ic-scl-2 -> vcc-2
- R80 pad 1: vcc-1 -> ch6.motor_driver.driver-_shunt_high
- R80 pad 2: i2c_mux.ic-sda-2 -> gnd
- R81 pad 1: vcc-1 -> ch6.motor_driver.driver-_shunt_high
- R81 pad 2: i2c_mux.ic-scl-3 -> ch6.motor_driver.op_amp-in1_plus
- R82 pad 1: vcc-1 -> ch6.motor_driver-current
- R82 pad 2: i2c_mux.ic-sda-3 -> ch6.motor_driver.op_amp-in1_minus
- R83 pad 1: vcc-1 -> ch6.motor_driver.op_amp-in1_minus
- R83 pad 2: i2c_mux.ic-scl-4 -> ch6.motor_driver._shunt_nettie-_shunt_gnd
- R84 pad 1: vcc-1 -> ch6.motor_driver-current
- R84 pad 2: i2c_mux.ic-sda-4 -> ch6.motor_driver.op_amp-in2_minus
- R85 pad 1: vcc-1 -> ch6.motor_driver.op_amp-in2_plus
- R85 pad 2: i2c_mux.ic-scl-5 -> vcc-2
- R86 pad 1: vcc-1 -> ch6.motor_driver.op_amp-in2_minus
- R86 pad 2: i2c_mux.ic-sda-5 -> gnd
- U1 pad 2: vcc-1 -> vcc-2
- U10 pad 5: vcc-1 -> vcc-2
- U11 pad 1: vcc -> gnd
- U11 pad 2: ch1.driver-out1 -> gnd
- U11 pad 3: ch1.driver-out2 -> reset_
- U11 pad 4: ch1.driver-_shunt_high -> i2c_mux.ic-sda
- U11 pad 5: ch1.pwm -> i2c_mux.ic-scl
- U11 pad 6: ch1.dir -> i2c_mux.ic-sda-1
- U11 pad 7: vcc-1 -> i2c_mux.ic-scl-1
- U11 pad 8: vcc-1 -> i2c_mux.ic-sda-2
- U11 pad 9: ch1.driver-ep -> i2c_mux.ic-scl-2
- U12 pad 1: ch1.driver-out1 -> vcc
- U12 pad 2: ch1.driver-out2 -> ch1.motor_driver.driver-out1
- U12 pad 3: (no net) -> ch1.motor_driver.driver-out2
- U12 pad 4: (no net) -> ch1.motor_driver.driver-_shunt_high
- U13 pad 1: ch1._shunt_nettie-_shunt_gnd -> ch1.motor_driver.driver-out1
- U13 pad 2: gnd -> ch1.motor_driver.driver-out2
- U14 pad 1: ch1.current -> ch1.motor_driver._shunt_nettie-_shunt_gnd
- U14 pad 2: ch1.op_amp-in1_minus -> gnd
- U16 pad 1: vcc -> vcc-1
- U16 pad 2: ch2.driver-out1 -> ch1.led.ic-led_dout
- U16 pad 3: ch2.driver-out2 -> gnd
- U16 pad 4: ch2.driver-_shunt_high -> uc._led.ic-led_dout
- U17 pad 1: ch2.driver-out1 -> vcc
- U17 pad 2: ch2.driver-out2 -> ch2.motor_driver.driver-out1
- U17 pad 3: (no net) -> ch2.motor_driver.driver-out2
- U17 pad 4: (no net) -> ch2.motor_driver.driver-_shunt_high
- U18 pad 1: ch2._shunt_nettie-_shunt_gnd -> ch2.motor_driver.driver-out1
- U18 pad 2: gnd -> ch2.motor_driver.driver-out2
- U19 pad 1: ch2.current -> ch2.motor_driver._shunt_nettie-_shunt_gnd
- U19 pad 2: ch2.op_amp-in1_minus -> gnd
- U21 pad 1: vcc -> vcc-1
- U21 pad 2: ch3.driver-out1 -> ch2.led.ic-led_dout
- U21 pad 3: ch3.driver-out2 -> gnd
- U21 pad 4: ch3.driver-_shunt_high -> ch1.led.ic-led_dout
- U22 pad 1: ch3.driver-out1 -> vcc
- U22 pad 2: ch3.driver-out2 -> ch3.motor_driver.driver-out1
- U22 pad 3: (no net) -> ch3.motor_driver.driver-out2
- U22 pad 4: (no net) -> ch3.motor_driver.driver-_shunt_high
- U23 pad 1: ch3._shunt_nettie-_shunt_gnd -> ch3.motor_driver.driver-out1
- U23 pad 2: gnd -> ch3.motor_driver.driver-out2
- U24 pad 1: ch3-current -> ch3.motor_driver._shunt_nettie-_shunt_gnd
- U24 pad 2: ch3.op_amp-in1_minus -> gnd
- U25 pad 1: vcc -> ch3.motor_driver-current
- U25 pad 2: ch4.driver-out1 -> ch3.motor_driver.op_amp-in1_minus
- U25 pad 3: ch4.driver-out2 -> ch3.motor_driver.op_amp-in1_plus
- U25 pad 4: ch4.driver-_shunt_high -> vcc-2
- U25 pad 5: ch4.pwm -> ch3.motor_driver.op_amp-in2_plus
- U25 pad 6: ch4.dir -> ch3.motor_driver.op_amp-in2_minus
- U25 pad 7: vcc-1 -> ch3.pulses
- U25 pad 8: vcc-1 -> ch3.motor_driver.op_amp-out3
- U26 pad 1: ch4.driver-out1 -> vcc-1
- U26 pad 2: ch4.driver-out2 -> ch3.led.ic-led_dout
- U26 pad 3: (no net) -> gnd
- U26 pad 4: (no net) -> ch2.led.ic-led_dout
- U27 pad 1: ch4._shunt_nettie-_shunt_gnd -> vcc
- U27 pad 2: gnd -> ch4.motor_driver.driver-out1
- U28 pad 1: ch4-current -> ch4.motor_driver.driver-out1
- U28 pad 2: ch4.op_amp-in1_minus -> ch4.motor_driver.driver-out2
- U28 pad 3: ch4.op_amp-in1_plus -> (no net)
- U28 pad 4: vcc-1 -> (no net)
- U29 pad 1: vcc -> ch4.motor_driver._shunt_nettie-_shunt_gnd
- U29 pad 2: ch5.driver-out1 -> gnd
- U3 pad 1: vcc-1 -> vcc-2
- U30 pad 1: ch5.driver-out1 -> ch4.motor_driver-current
- U30 pad 2: ch5.driver-out2 -> ch4.motor_driver.op_amp-in1_minus
- U30 pad 3: (no net) -> ch4.motor_driver.op_amp-in1_plus
- U30 pad 4: (no net) -> vcc-2
- U31 pad 1: ch5._shunt_nettie-_shunt_gnd -> vcc-1
- U31 pad 2: gnd -> ch4.led.ic-led_dout
- U32 pad 1: ch5-current -> vcc
- U32 pad 2: ch5.op_amp-in1_minus -> ch5.motor_driver.driver-out1
- U32 pad 3: ch5.op_amp-in1_plus -> ch5.motor_driver.driver-out2
- U32 pad 4: vcc-1 -> ch5.motor_driver.driver-_shunt_high
- U32 pad 5: ch5.op_amp-in2_plus -> ch5.pwm
- U32 pad 6: ch5.op_amp-in2_minus -> ch5.dir
- U32 pad 7: ch5.pulses -> vcc-2
- U32 pad 8: ch5.op_amp-out3 -> ch5.motor_driver-enable
- U33 pad 1: vcc -> ch5.motor_driver.driver-out1
- U33 pad 2: ch6.driver-out1 -> ch5.motor_driver.driver-out2
- U33 pad 3: ch6.driver-out2 -> (no net)
- U33 pad 4: ch6.driver-_shunt_high -> (no net)
- U34 pad 1: ch6.driver-out1 -> ch5.motor_driver._shunt_nettie-_shunt_gnd
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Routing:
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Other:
- board text added: "chx"
